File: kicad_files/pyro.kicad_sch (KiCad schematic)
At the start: 7 parts, among them J9 IGN_1, Q3 AO3400A

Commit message: reset symbol annotations
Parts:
- renumbered R29 to R26, R30 to R27, R31 to R28, R32 to R29
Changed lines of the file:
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@@
 		(in_pos_files yes)
 		(dnp no)
-		(property "Reference" "R29"
+		(property "Reference" "R26"
 			(at 140.97 40.64 0)
 			(show_name no)
@@
 			(project "versorlite"
 				(path "/1a230af0-0a74-48f7-8607-b087121dda49/f02bd2f9-723f-45ac-a652-42be6cba2a93"
-					(reference "R29")
+					(reference "R26")
 					(unit 1)
 				)
@@
 		(in_pos_files yes)
 		(dnp no)
-		(property "Reference" "R30"
+		(property "Reference" "R27"
 			(at 140.97 59.69 0)
 			(show_name no)
@@
 			(project "versorlite"
 				(path "/1a230af0-0a74-48f7-8607-b087121dda49/f02bd2f9-723f-45ac-a652-42be6cba2a93"
-					(reference "R30")
+					(reference "R27")
 					(unit 1)
 				)
@@
 		(in_pos_files yes)
 		(dnp no)
-		(property "Reference" "R32"
+		(property "Reference" "R29"
 			(at 165.1 53.34 90)
 			(show_name no)
@@
 			(project "versorlite"
 				(path "/1a230af0-0a74-48f7-8607-b087121dda49/f02bd2f9-723f-45ac-a652-42be6cba2a93"
-					(reference "R32")
+					(reference "R29")
 					(unit 1)
 				)
@@
 		(in_pos_files yes)
 		(dnp no)
-		(property "Reference" "R31"
+		(property "Reference" "R28"
 			(at 156.21 50.8 0)
 			(show_name no)
@@
 			(project "versorlite"
 				(path "/1a230af0-0a74-48f7-8607-b087121dda49/f02bd2f9-723f-45ac-a652-42be6cba2a93"
-					(reference "R31")
-					(unit 1)
-				)
+					(reference "R28")
+					(unit 1)
+				)

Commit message: make schematic changes
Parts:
- D7: value D_Schottky_Small -> CUS10S30,H3F; footprint (none) -> Diode_SMD:D_SOD-323
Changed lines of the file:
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@@
 			)
 		)
-		(property "Value" "D_Schottky_Small"
+		(property "Value" "CUS10S30,H3F"
 			(at 138.43 56.134 90)
 			(show_name no)
@@
 			)
 		)
-		(property "Footprint" ""
+		(property "Footprint" "Diode_SMD:D_SOD-323"
 			(at 135.89 54.61 90)
 			(hide yes)

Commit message: Rearrange PCB
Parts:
- J9: footprint (none) -> TerminalBlock_Phoenix:TerminalBlock_Phoenix_PTSM-0,5-2-2,5-V-SMD_1x02-1MP_P2.50mm_Vertical
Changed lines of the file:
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@@
 			)
 		)
-		(property "Footprint" ""
+		(property "Footprint" "TerminalBlock_Phoenix:TerminalBlock_Phoenix_PTSM-0,5-2-2,5-V-SMD_1x02-1MP_P2.50mm_Vertical"
 			(at 125.73 72.39 0)
 			(hide yes)

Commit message: Use more robust terminal block
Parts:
- J9: footprint TerminalBlock_Phoenix:TerminalBlock_Phoenix_PTSM-0,5-2-2,5-V-SMD_1x02-1MP_P2.50mm_Vertical -> TerminalBlock_Phoenix:TerminalBlock_Phoenix_PTSM-0,5-2-2.5-H-THR_1x02_P2.50mm_Horizontal
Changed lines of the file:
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@@
 			)
 		)
-		(property "Footprint" "TerminalBlock_Phoenix:TerminalBlock_Phoenix_PTSM-0,5-2-2,5-V-SMD_1x02-1MP_P2.50mm_Vertical"
+		(property "Footprint" "TerminalBlock_Phoenix:TerminalBlock_Phoenix_PTSM-0,5-2-2.5-H-THR_1x02_P2.50mm_Horizontal"
 			(at 125.73 72.39 0)
 			(hide yes)

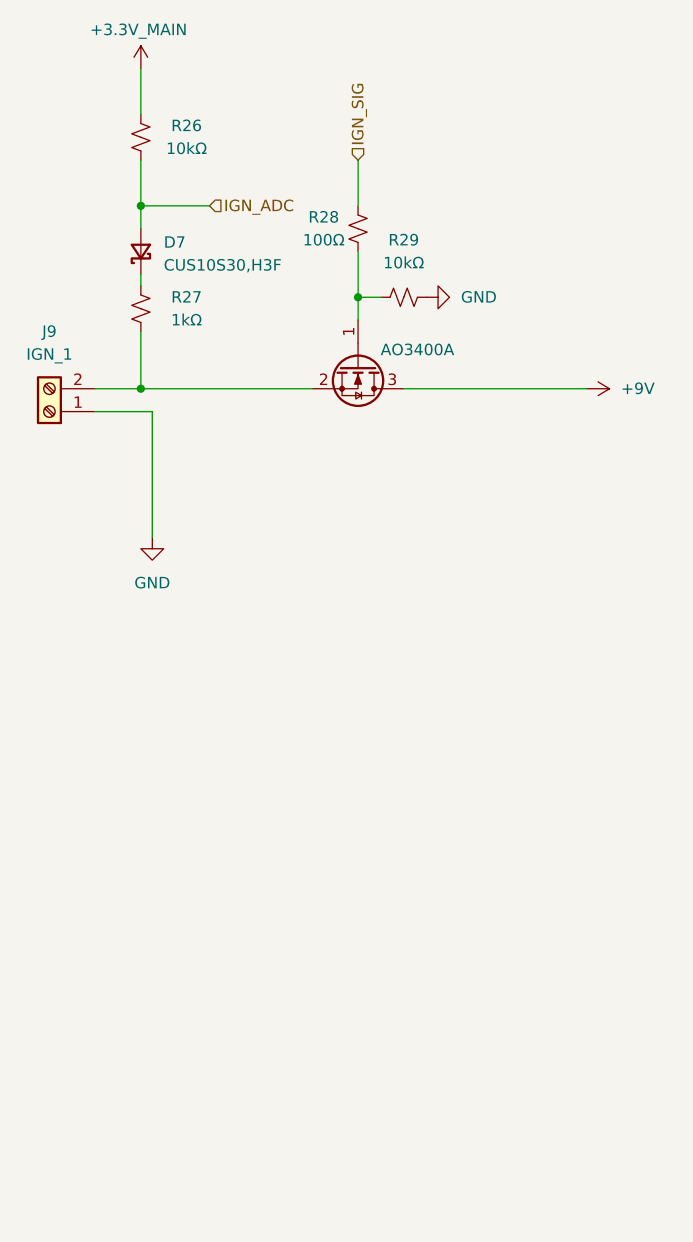
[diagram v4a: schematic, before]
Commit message: Add second pyro channel
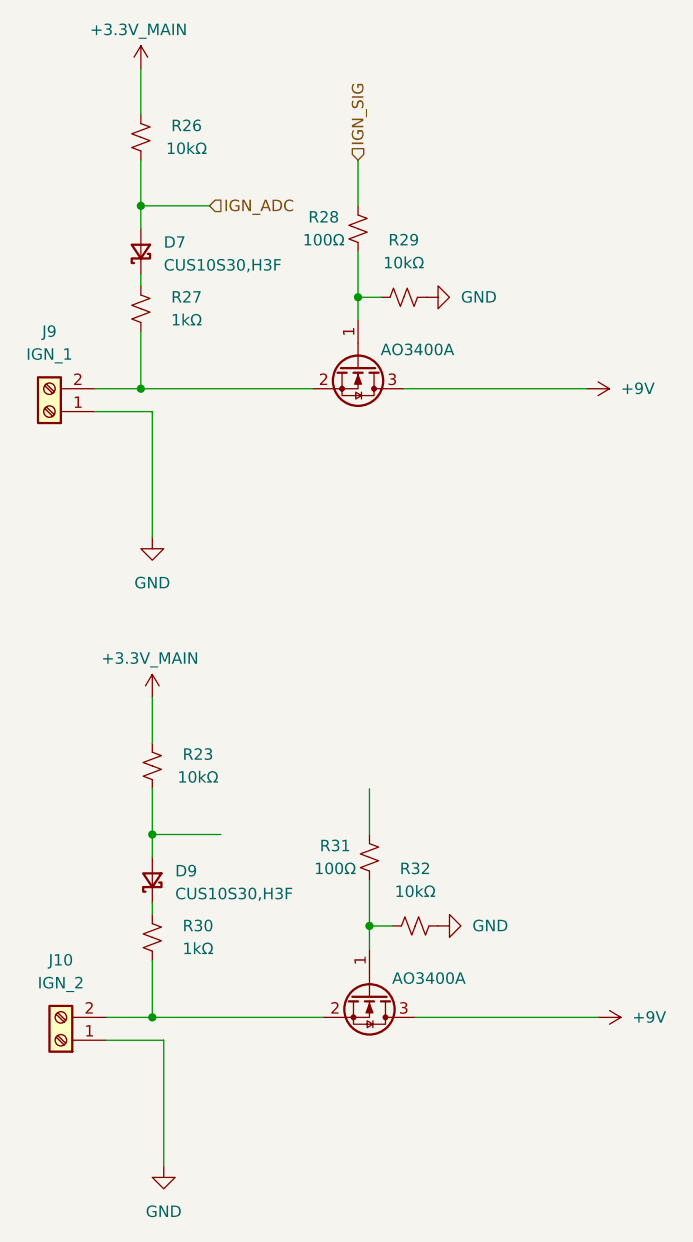
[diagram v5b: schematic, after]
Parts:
- added D9: CUS10S30,H3F, Diode_SMD:D_SOD-323, symbol Device:D_Schottky_Small
- added J10: IGN_2, Connector_Wire:SolderWire-0.5sqmm_1x02_P4.6mm_D0.9mm_OD2.1mm, symbol Connector:Screw_Terminal_01x02
- added Q2: AO3400A, Package_TO_SOT_SMD:SOT-23, symbol Transistor_FET:AO3400A
- added R23, R32: 10kΩ, Resistor_SMD:R_0402_1005Metric, symbol Device:R_Small_US
- added R30: 1kΩ, Resistor_SMD:R_0805_2012Metric, symbol Device:R_Small_US
- added R31: 100Ω, Resistor_SMD:R_0603_1608Metric, symbol Device:R_Small_US
- J9: footprint TerminalBlock_Phoenix:TerminalBlock_Phoenix_PTSM-0,5-2-2.5-H-THR_1x02_P2.50mm_Horizontal -> Connector_Wire:SolderWire-0.5sqmm_1x02_P4.6mm_D0.9mm_OD2.1mm
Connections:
- net +3.3V_MAIN: now also R23.1
- net +9V: now also Q2.3 (D)
- net GND: now also J10.1 (Pin_1), R32.2
- new net: J10.2 (Pin_2), Q2.2 (S), R30.2
- new net: Q2.1 (G), R31.1, R32.1
- new net: D9.1 (K), R30.1
- new net: D9.2 (A), R23.2

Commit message: Connect IGN2 signal, rearrange
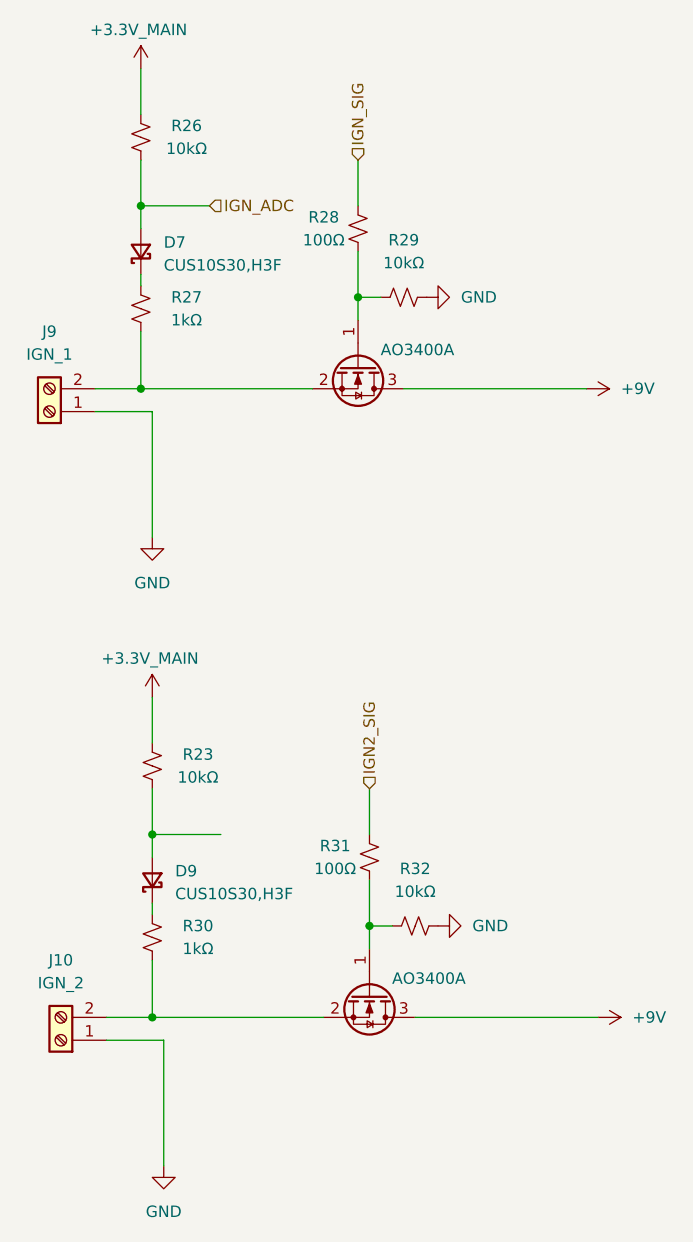
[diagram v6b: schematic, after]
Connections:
- net IGN2_SIG: now reaches R31.2
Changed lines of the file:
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@@
+		)
+	)
+	(hierarchical_label "IGN2_SIG"
+		(shape input)
+		(at 161.29 114.3 90)
+		(effects
+			(font
+				(size 1.27 1.27)
+			)
+			(justify left)
 		)
 	)

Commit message: add dedicated power switching
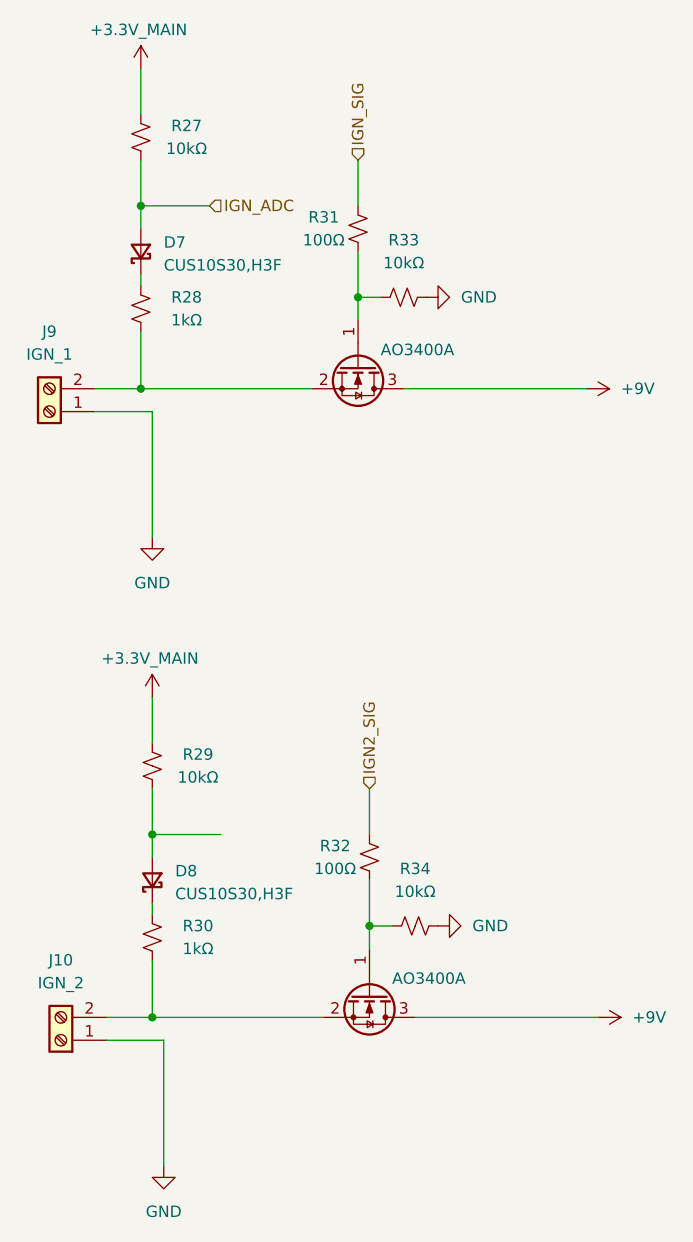
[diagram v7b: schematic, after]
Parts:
- renumbered D9 to D8, Q3 to Q1, R26 to R27, R27 to R28, R23 to R29, R28 to R31, R31 to R32, R29 to R33, R32 to R34
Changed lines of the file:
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@@
 		(in_pos_files yes)
 		(dnp no)
-		(property "Reference" "R26"
+		(property "Reference" "R27"
 			(at 140.97 40.64 0)
 			(show_name no)
@@
 			(project "versorlite"
 				(path "/1a230af0-0a74-48f7-8607-b087121dda49/f02bd2f9-723f-45ac-a652-42be6cba2a93"
-					(reference "R26")
+					(reference "R27")
 					(unit 1)
 				)
@@
 		(dnp no)
 		(fields_autoplaced yes)
-		(property "Reference" "#PWR094"
+		(property "Reference" "#PWR097"
 			(at 173.99 59.69 0)
 			(hide yes)
@@
 			(project "versorlite"
 				(path "/1a230af0-0a74-48f7-8607-b087121dda49/f02bd2f9-723f-45ac-a652-42be6cba2a93"
-					(reference "#PWR094")
+					(reference "#PWR097")
 					(unit 1)
 				)
@@
 		(dnp no)
 		(fields_autoplaced yes)
-		(property "Reference" "#PWR049"
+		(property "Reference" "#PWR096"
 			(at 138.43 162.56 0)
 			(hide yes)
@@
 			(project "versorlite"
 				(path "/1a230af0-0a74-48f7-8607-b087121dda49/f02bd2f9-723f-45ac-a652-42be6cba2a93"
-					(reference "#PWR049")
+					(reference "#PWR096")
 					(unit 1)
 				)
@@
 		(dnp no)
 		(fields_autoplaced yes)
-		(property "Reference" "#PWR095"
+		(property "Reference" "#PWR099"
 			(at 181.61 69.85 0)
 			(hide yes)
@@
 			(project "versorlite"
 				(path "/1a230af0-0a74-48f7-8607-b087121dda49/f02bd2f9-723f-45ac-a652-42be6cba2a93"
-					(reference "#PWR095")
+					(reference "#PWR099")
 					(unit 1)
 				)
@@
 		(dnp no)
 		(fields_autoplaced yes)
-		(property "Reference" "#PWR093"
+		(property "Reference" "#PWR094"
 			(at 137.16 92.71 0)
 			(hide yes)
@@
 			(project "versorlite"
 				(path "/1a230af0-0a74-48f7-8607-b087121dda49/f02bd2f9-723f-45ac-a652-42be6cba2a93"
-					(reference "#PWR093")
+					(reference "#PWR094")
 					(unit 1)
 				)
@@
 		(in_pos_files yes)
 		(dnp no)
-		(property "Reference" "#PWR092"
+		(property "Reference" "#PWR093"
 			(at 135.89 38.1 0)
 			(hide yes)
@@
 			(project "versorlite"
 				(path "/1a230af0-0a74-48f7-8607-b087121dda49/f02bd2f9-723f-45ac-a652-42be6cba2a93"
-					(reference "#PWR092")
+					(reference "#PWR093")
 					(unit 1)
 				)
@@
 		(dnp no)
 		(fields_autoplaced yes)
-		(property "Reference" "#PWR050"
+		(property "Reference" "#PWR098"
 			(at 175.26 129.54 0)
 			(hide yes)
@@
 			(project "versorlite"
 				(path "/1a230af0-0a74-48f7-8607-b087121dda49/f02bd2f9-723f-45ac-a652-42be6cba2a93"
-					(reference "#PWR050")
+					(reference "#PWR098")
 					(unit 1)
 				)
@@
 		(in_pos_files yes)
 		(dnp no)
-		(property "Reference" "Q3"
+		(property "Reference" "Q1"
 			(at 160.02 73.66 90)
 			(hide yes)
@@
 			(project "versorlite"
 				(path "/1a230af0-0a74-48f7-8607-b087121dda49/f02bd2f9-723f-45ac-a652-42be6cba2a93"
-					(reference "Q3")
+					(reference "Q1")
 					(unit 1)
 				)
@@
 		(in_pos_files yes)
 		(dnp no)
-		(property "Reference" "#PWR048"
+		(property "Reference" "#PWR095"
 			(at 137.16 107.95 0)
 			(hide yes)
@@
 			(project "versorlite"
 				(path "/1a230af0-0a74-48f7-8607-b087121dda49/f02bd2f9-723f-45ac-a652-42be6cba2a93"
-					(reference "#PWR048")
+					(reference "#PWR095")
 					(unit 1)
 				)
@@
 		(in_pos_files yes)
 		(dnp no)
-		(property "Reference" "D9"
+		(property "Reference" "D8"
 			(at 139.7 123.4439 90)
 			(show_name no)
@@
 			(project "versorlite"
 				(path "/1a230af0-0a74-48f7-8607-b087121dda49/f02bd2f9-723f-45ac-a652-42be6cba2a93"
-					(reference "D9")
+					(reference "D8")
 					(unit 1)
 				)
@@
 		(in_pos_files yes)
 		(dnp no)
-		(property "Reference" "R31"
+		(property "Reference" "R32"
 			(at 157.48 120.65 0)
 			(show_name no)
@@
 			(project "versorlite"
 				(path "/1a230af0-0a74-48f7-8607-b087121dda49/f02bd2f9-723f-45ac-a652-42be6cba2a93"
-					(reference "R31")
+					(reference "R32")
 					(unit 1)
 				)
@@
 		(in_pos_files yes)
 		(dnp no)
-		(property "Reference" "R23"
+		(property "Reference" "R29"
 			(at 142.24 110.49 0)
 			(show_name no)
@@
 			(project "versorlite"
 				(path "/1a230af0-0a74-48f7-8607-b087121dda49/f02bd2f9-723f-45ac-a652-42be6cba2a93"
-					(reference "R23")
+					(reference "R29")
 					(unit 1)
 				)
@@
 		(in_pos_files yes)
 		(dnp no)
-		(property "Reference" "R32"
+		(property "Reference" "R34"
 			(at 166.37 123.19 90)
 			(show_name no)
@@
 			(project "versorlite"
 				(path "/1a230af0-0a74-48f7-8607-b087121dda49/f02bd2f9-723f-45ac-a652-42be6cba2a93"
-					(reference "R32")
+					(reference "R34")
 					(unit 1)
 				)
@@
 		(in_pos_files yes)
 		(dnp no)
-		(property "Reference" "R27"
+		(property "Reference" "R28"
 			(at 140.97 59.69 0)
 			(show_name no)
@@
 			(project "versorlite"
 				(path "/1a230af0-0a74-48f7-8607-b087121dda49/f02bd2f9-723f-45ac-a652-42be6cba2a93"
-					(reference "R27")
+					(reference "R28")
 					(unit 1)
 				)
@@
 		(dnp no)
 		(fields_autoplaced yes)
-		(property "Reference" "#PWR051"
+		(property "Reference" "#PWR0100"
 			(at 182.88 139.7 0)
 			(hide yes)
@@
 			(project "versorlite"
 				(path "/1a230af0-0a74-48f7-8607-b087121dda49/f02bd2f9-723f-45ac-a652-42be6cba2a93"
-					(reference "#PWR051")
+					(reference "#PWR0100")
 					(unit 1)
 				)
@@
 		(in_pos_files yes)
 		(dnp no)
-		(property "Reference" "R29"
+		(property "Reference" "R33"
 			(at 165.1 53.34 90)
 			(show_name no)
@@
 			(project "versorlite"
 				(path "/1a230af0-0a74-48f7-8607-b087121dda49/f02bd2f9-723f-45ac-a652-42be6cba2a93"
-					(reference "R29")
+					(reference "R33")
 					(unit 1)
 				)
@@
 		(in_pos_files yes)
 		(dnp no)
-		(property "Reference" "R28"
+		(property "Reference" "R31"
 			(at 156.21 50.8 0)
 			(show_name no)
@@
 			(project "versorlite"
 				(path "/1a230af0-0a74-48f7-8607-b087121dda49/f02bd2f9-723f-45ac-a652-42be6cba2a93"
-					(reference "R28")
-					(unit 1)
-				)
+					(reference "R31")
+					(unit 1)
+				)

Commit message: add ign_adc2
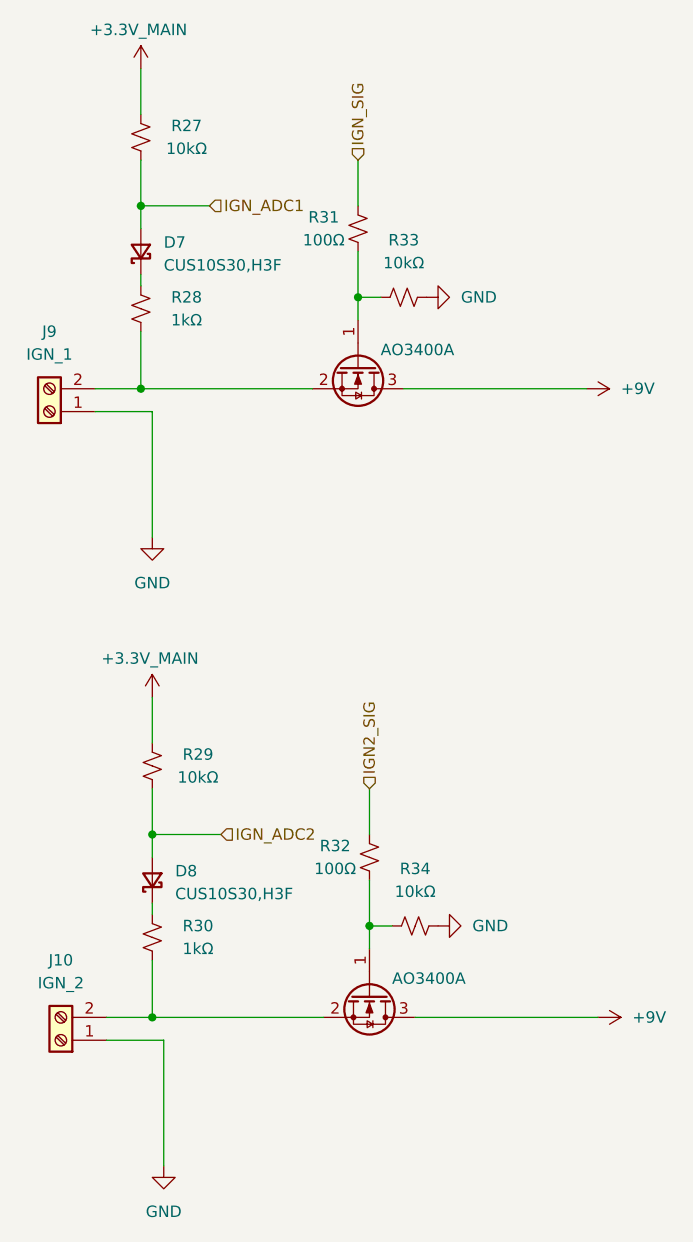
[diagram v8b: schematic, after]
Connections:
- net IGN_ADC2: now reaches D8.2 (A), R29.2
- net IGN_ADC renamed IGN_ADC1
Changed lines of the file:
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@@
 		)
 	)
-	(hierarchical_label "IGN_ADC"
+	(hierarchical_label "IGN_ADC1"
 		(shape input)
 		(at 143.51 49.53 0)
 		(effects
 			(font
+				(size 1.27 1.27)
+			)
+			(justify left)
+		)
+	)
+	(hierarchical_label "IGN_ADC2"
+		(shape input)
+		(at 144.78 119.38 0)
+		(effects
+			(font
